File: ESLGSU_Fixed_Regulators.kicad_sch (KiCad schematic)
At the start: 0 parts

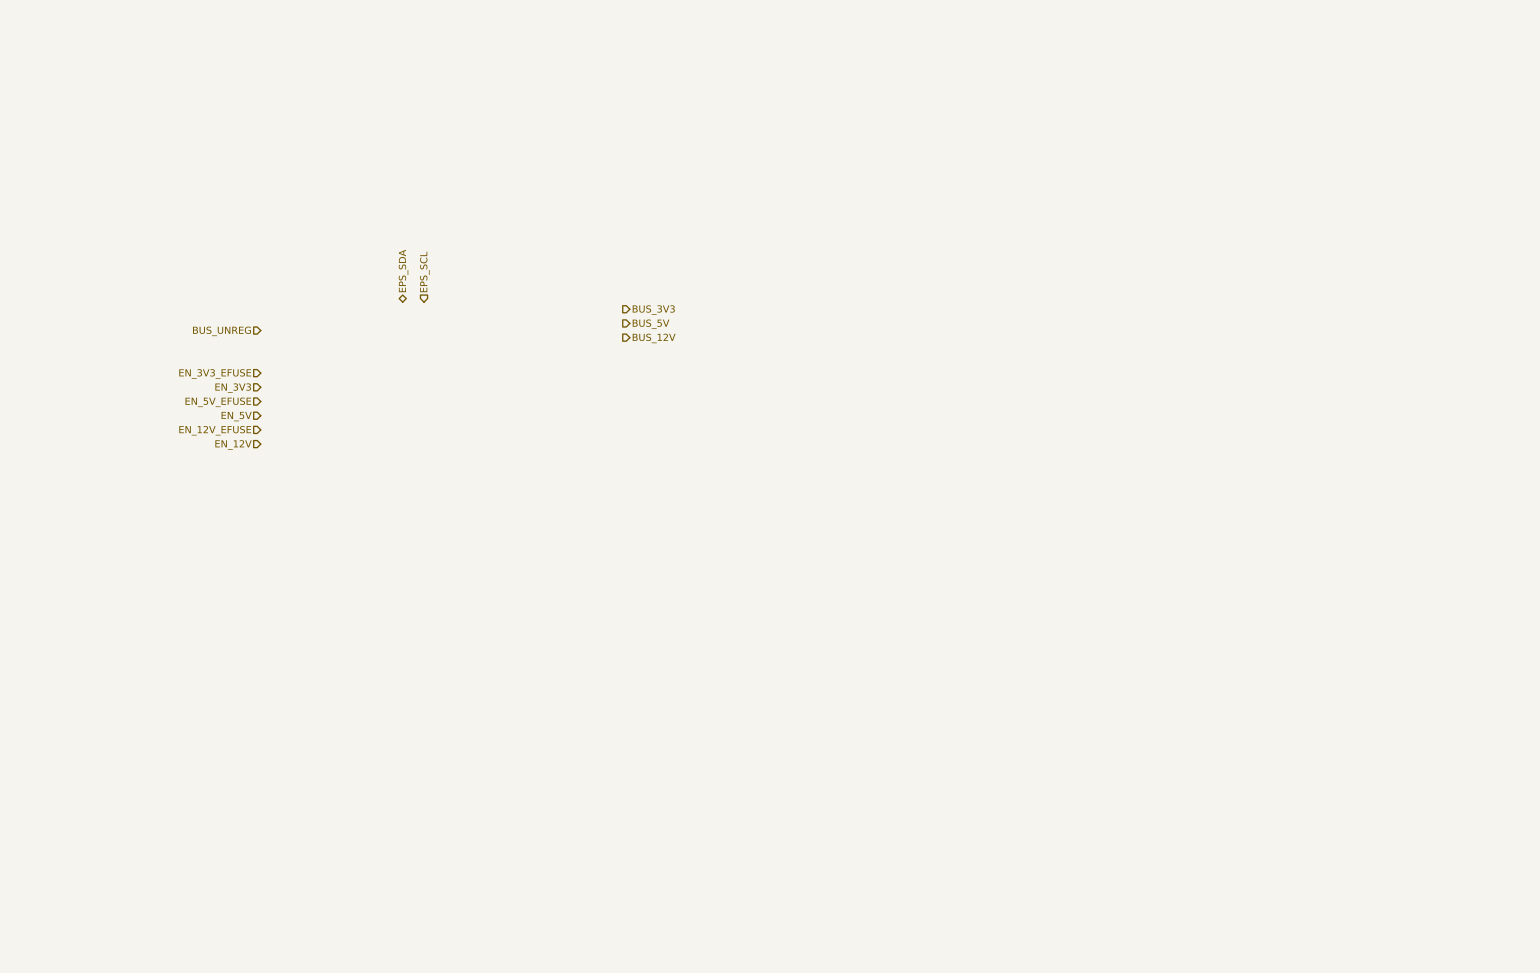
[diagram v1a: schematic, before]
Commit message: Additional power regulation work
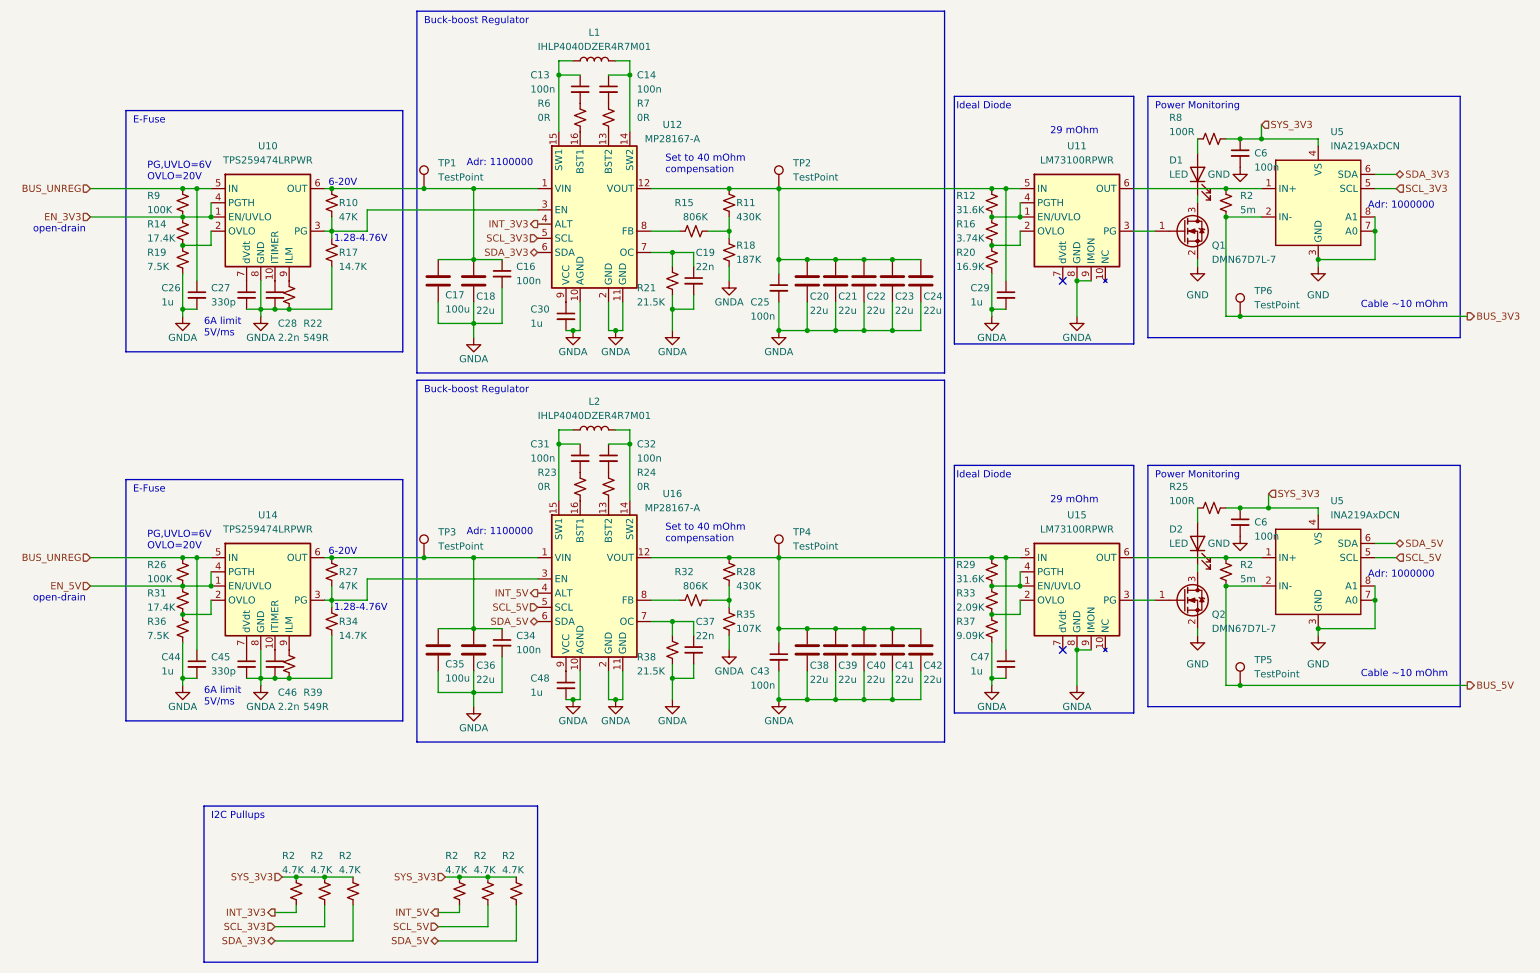
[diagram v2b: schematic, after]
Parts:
- added C13, C14, C16, C25, C31, C32, C34, C43, C6 (x2): 100n, Capacitor_SMD:C_0603_1608Metric, symbol Device:C_Small
- added C17, C35: 100u, Capacitor_SMD:CP_Elec_6.3x7.7, symbol Device:C
- added C18, C20, C21, C22, C23, C24, C36, C38, C39, C40, C41, C42: 22u, Capacitor_SMD:C_0805_2012Metric, symbol Device:C
- added C19, C37: 22n, Capacitor_SMD:C_0603_1608Metric, symbol Device:C_Small
- added C26, C29, C30, C44, C47, C48: 1u, Capacitor_SMD:C_0603_1608Metric, symbol Device:C_Small
- added C27, C45: 330p, Capacitor_SMD:C_0603_1608Metric, symbol Device:C_Small
- added C28, C46: 2.2n, Capacitor_SMD:C_0603_1608Metric, symbol Device:C_Small
- added D1, D2: LED, LED_SMD:LED_0603_1608Metric, symbol Device:LED
- added L1, L2: IHLP4040DZER4R7M01, Inductor_SMD:L_Vishay_IHLP-4040, symbol Device:L
- added Q1, Q2: DMN67D7L-7, Package_TO_SOT_SMD:SOT-323_SC-70, symbol Transistor_FET:DMN67D7L
- added R10, R27: 47K, Resistor_SMD:R_0603_1608Metric, symbol Device:R_Small_US
- added R11, R28: 430K, Resistor_SMD:R_0603_1608Metric, symbol Device:R_Small_US
- added R12, R29: 31.6K, Resistor_SMD:R_0603_1608Metric, symbol Device:R_Small_US
- added R14, R31: 17.4K, Resistor_SMD:R_0603_1608Metric, symbol Device:R_Small_US
- added R15, R32: 806K, Resistor_SMD:R_0603_1608Metric, symbol Device:R_Small_US
- added R16: 3.74K, Resistor_SMD:R_0603_1608Metric, symbol Device:R_Small_US
- added R17, R34: 14.7K, Resistor_SMD:R_0603_1608Metric, symbol Device:R_Small_US
- added R18: 187K, Resistor_SMD:R_0603_1608Metric, symbol Device:R_Small_US
- added R19, R36: 7.5K, Resistor_SMD:R_0603_1608Metric, symbol Device:R_Small_US
- added R2 (x6): 4.7K, Resistor_SMD:R_0603_1608Metric, symbol Device:R_Small_US
- added R2 (x2): 5m, Resistor_SMD:R_0603_1608Metric, symbol Device:R_Small_US
- added R20: 16.9K, Resistor_SMD:R_0603_1608Metric, symbol Device:R_Small_US
- added R21, R38: 21.5K, Resistor_SMD:R_0603_1608Metric, symbol Device:R_Small_US
- added R22, R39: 549R, Resistor_SMD:R_0603_1608Metric, symbol Device:R_Small_US
- added R23, R24, R6, R7: 0R, Resistor_SMD:R_0603_1608Metric, symbol Device:R_Small_US
- added R25, R8: 100R, Resistor_SMD:R_0603_1608Metric, symbol Device:R_Small_US
- added R26, R9: 100K, Resistor_SMD:R_0603_1608Metric, symbol Device:R_Small_US
- added R33: 2.09K, Resistor_SMD:R_0603_1608Metric, symbol Device:R_Small_US
- added R35: 107K, Resistor_SMD:R_0603_1608Metric, symbol Device:R_Small_US
- added R37: 9.09K, Resistor_SMD:R_0603_1608Metric, symbol Device:R_Small_US
- added TP1, TP2, TP3, TP4, TP5, TP6: TestPoint, TestPoint:TestPoint_Pad_D2.0mm, symbol Connector:TestPoint
- added U10, U14: TPS259474LRPWR, ESLGSU_Parts_Lib:VQFN-HR, symbol ESLGSU_Parts_Lib:TPS259474ARPWR
- added U11, U15: LM73100RPWR, ESLGSU_Parts_Lib:VQFN-HR, symbol ESLGSU_Parts_Lib:LM73100
- added U12, U16: MP28167-A, ESLGSU_Parts_Lib:QFN-16-MP28167, symbol ESLGSU_Parts_Lib:MP28167-A
- added U5 (x2): INA219AxDCN, Package_TO_SOT_SMD:SOT-23-8, symbol Sensor_Energy:INA219AxDCN
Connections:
- net BUS_3V3: now also R2.2, TP6.1, U5.2 (IN-)
- net BUS_5V: now also R2.2, TP5.1, U5.2 (IN-)
- net BUS_UNREG: now also C26.1, C44.1, R26.1, R9.1, U10.5 (IN), U14.5 (IN)
- net EN_3V3: now also R14.1, R9.2, U10.1 (EN/UVLO), U10.4 (PGTH)
- net EN_5V: now also R26.2, R31.1, U14.1 (EN/UVLO), U14.4 (PGTH)
- new net: C14.1, L1.2, U12.14 (SW2)
- new net: C14.2, R7.1
- new net: C20.1, C21.1, C22.1, C23.1, C24.1, C25.1, C29.1, R11.1, R12.1, TP2.1, U11.5 (IN), U12.12 (VOUT)
- new net: R11.2, R15.2, R18.1
- new net: C27.1, U10.7 (dVdt)
- new net: C13.1, L1.1, U12.15 (SW1)
- new net: C38.1, C39.1, C40.1, C41.1, C42.1, C43.1, C47.1, R28.1, R29.1, TP4.1, U15.5 (IN), U16.12 (VOUT)
- new net: C34.1, C35.1, C36.1, R27.1, TP3.1, U14.6 (OUT), U16.1 (VIN)
- new net: R31.2, R36.1, U14.2 (OVLO)
- new net: C13.2, R6.1
- new net: C16.1, C17.1, C18.1, R10.1, TP1.1, U10.6 (OUT), U12.1 (VIN)
- new net: R14.2, R19.1, U10.2 (OVLO)
- new net: R10.2, R17.1, U10.3 (PG), U12.3 (EN)
- new net: C31.1, L2.1, U16.15 (SW1)
- new net: C32.1, L2.2, U16.14 (SW2)
- new net: D2.2 (A), R25.2
- new net: C28.1, U10.10 (ITIMER)
- new net: C48.1, U16.9 (VCC)
- new net: R2.1, U11.6 (OUT), U5.1 (IN+)
- new net: R7.2, U12.13 (BST2)
- new net: R2.1, U15.6 (OUT), U5.1 (IN+)
- new net: R12.2, R16.1, U11.1 (EN/UVLO), U11.4 (PGTH)
- new net: R16.2, R20.1, U11.2 (OVLO)
- new net: R22.1, U10.9 (ILM)
- new net: R39.1, U14.9 (ILM)
- new net: R28.2, R32.2, R35.1
- new net: D1.2 (A), R8.2
- new net: R27.2, R34.1, U14.3 (PG), U16.3 (EN)
- new net: C30.1, U12.9 (VCC)
- new net: C19.1, R21.1, U12.7 (OC)
- new net: D2.1 (K), Q2.3 (D)
- new net: Q1.1 (G), U11.3 (PG)
- new net: C46.1, U14.10 (ITIMER)
- new net: C32.2, R24.1
- new net: R24.2, U16.13 (BST2)
- new net: R23.2, U16.16 (BST1)
- new net: C37.1, R38.1, U16.7 (OC)
- new net: R32.1, U16.8 (FB)
- new net: R6.2, U12.16 (BST1)
- new net: R15.1, U12.8 (FB)
- new net: C31.2, R23.1
- new net: D1.1 (K), Q1.3 (D)
- new net: R29.2, R33.1, U15.1 (EN/UVLO), U15.4 (PGTH)
- new net: R33.2, R37.1, U15.2 (OVLO)
- new net: Q2.1 (G), U15.3 (PG)
- new net: C45.1, U14.7 (dVdt)
- new net GND: C6.2, C6.2, Q1.2 (S), Q2.2 (S), U5.3 (GND), U5.3 (GND), U5.7 (A0), U5.7 (A0), U5.8 (A1), U5.8 (A1)
- new net GNDA: C16.2, C17.2, C18.2, C19.2, C20.2, C21.2, C22.2, C23.2, C24.2, C25.2, C26.2, C27.2, C28.2, C29.2, C30.2, C34.2, C35.2, C36.2, C37.2, C38.2, C39.2, C40.2, C41.2, C42.2, C43.2, C44.2, C45.2, C46.2, C47.2, C48.2, R17.2, R18.2, R19.2, R20.2, R21.2, R22.2, R34.2, R35.2, R36.2, R37.2, R38.2, R39.2, U10.8 (GND), U11.8 (GND), U11.9 (IMON), U12.10 (AGND), U12.11 (GND), U12.2 (GND), U14.8 (GND), U15.8 (GND), U15.9 (IMON), U16.10 (AGND), U16.11 (GND), U16.2 (GND)
- new net INT_3V3: R2.2, U12.4 (ALT)
- new net INT_5V: R2.2, U16.4 (ALT)
- new net SCL_3V3: R2.2, U12.5 (SCL), U5.5 (SCL)
- new net SCL_5V: R2.2, U16.5 (SCL), U5.5 (SCL)
- new net SDA_3V3: R2.2, U12.6 (SDA), U5.6 (SDA)
- new net SDA_5V: R2.2, U16.6 (SDA), U5.6 (SDA)
- new net SYS_3V3: C6.1, C6.1, R2.1, R2.1, R2.1, R2.1, R2.1, R2.1, R25.1, R8.1, U5.4 (VS), U5.4 (VS)
- no-connect marks 0 -> 2
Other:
- note added: "1.28-4.76V"
- note added: "29 mOhm"
- note added: "6-20V"
- note added: "6A limit 5V/ms"
- note added: "Adr: 1000000"
- note added: "Adr: 1100000"
- note added: "Buck-boost Regulator"
- note added: "Cable ~10 mOhm"
- note added: "E-Fuse"
- note added: "I2C Pullups"
- note added: "Ideal Diode"
- note added: "PG,UVLO=6V OVLO=20V"
- note added: "Power Monitoring"
- note added: "Set to 40 mOhm compensation"
- note added: "open-drain"

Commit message: Added 5v/3V3 regulators and mux
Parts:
- added R87, R88: 47K, Resistor_SMD:R_0603_1608Metric, symbol Device:R_Small_US
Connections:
- net at D2.2 (A), R25.2: now also R88.1
- net at D1.2 (A), R8.2: now also R87.1
- net at Q1.1 (G), U11.3 (PG): now also R87.2
- net at Q2.1 (G), U15.3 (PG): now also R88.2
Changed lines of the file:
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@@
   (junction (at 204.47 62.23) (diameter 0) (color 0 0 0 0)
   )
+  (junction (at 226.06 102.87) (diameter 0) (color 0 0 0 0)
+  )
   (junction (at 151.13 111.76) (diameter 0) (color 0 0 0 0)
   )
@@
   (junction (at 132.08 67.31) (diameter 0) (color 0 0 0 0)
   )
+  (junction (at 218.44 119.38) (diameter 0) (color 0 0 0 0)
+  )
   (junction (at 44.45 45.72) (diameter 0) (color 0 0 0 0)
   )
+  (junction (at 226.06 36.83) (diameter 0) (color 0 0 0 0)
+  )
   (junction (at 142.24 119.38) (diameter 0) (color 0 0 0 0)
   )
@@
   (junction (at 233.68 68.58) (diameter 0) (color 0 0 0 0)
   )
+  (junction (at 218.44 53.34) (diameter 0) (color 0 0 0 0)
+  )
   (junction (at 151.13 71.12) (diameter 0) (color 0 0 0 0)
   )
@@
     (stroke (width 0) (type default))
   )
+  (wire (pts (xy 220.98 36.83) (xy 218.44 36.83))
+    (stroke (width 0) (type default))
+  )
   (wire (pts (xy 231.14 50.8) (xy 237.49 50.8))
     (stroke (width 0) (type default))
@@
     (stroke (width 0) (type default))
   )
+  (wire (pts (xy 220.98 102.87) (xy 218.44 102.87))
+    (stroke (width 0) (type default))
+  )
   (wire (pts (xy 44.45 67.31) (xy 44.45 68.58))
     (stroke (width 0) (type default))
@@
     (stroke (width 0) (type default))
   )
+  (wire (pts (xy 218.44 102.87) (xy 218.44 119.38))
+    (stroke (width 0) (type default))
+  )
   (wire (pts (xy 231.14 36.83) (xy 233.68 36.83))
     (stroke (width 0) (type default))
@@
     (stroke (width 0) (type default))
   )
+  (wire (pts (xy 218.44 36.83) (xy 218.44 53.34))
+    (stroke (width 0) (type default))
+  )
   (wire (pts (xy 171.45 124.46) (xy 176.53 124.46))
     (stroke (width 0) (type default))
@@
     (effects (font (size 1.27 1.27)) (justify left))
   )
+  (symbol (lib_id "Device:R_Small_US") (at 223.52 36.83 270) (unit 1)
+    (in_bom yes) (on_board yes) (dnp no)
+    (property "Reference" "R87" (at 217.4449 32.9491 90)
+      (effects (font (size 1.27 1.27)) (justify left))
+    )
+    (property "Value" "47K" (at 217.4449 35.4891 90)
+      (effects (font (size 1.27 1.27)) (justify left))
+    )
+    (property "Footprint" "Resistor_SMD:R_0603_1608Metric" (at 223.52 36.83 0)
+      (effects (font (size 1.27 1.27)) hide)
+    )
+    (property "Datasheet" "~" (at 223.52 36.83 0)
+      (effects (font (size 1.27 1.27)) hide)
+    )
+    (pin "1")
+    (pin "2")
+    (instances
+      (project "ESLGSU"
+        (path "/b556fa32-e0cb-409c-ac85-9f2ac606be79/09a64186-e4de-4db7-b903-c6397ff9a54d"
+          (reference "R87") (unit 1)
+        )
+      )
+    )
+  )
   (symbol (lib_id "power:GNDA") (at 189.23 68.58 0) (unit 1)
     (in_bom yes) (on_board yes) (dnp no)
@@
     )
   )
+  (symbol (lib_id "Device:R_Small_US") (at 223.52 102.87 270) (unit 1)
+    (in_bom yes) (on_board yes) (dnp no)
+    (property "Reference" "R88" (at 217.4449 98.9891 90)
+      (effects (font (size 1.27 1.27)) (justify left))
+    )
+    (property "Value" "47K" (at 217.4449 101.5291 90)
+      (effects (font (size 1.27 1.27)) (justify left))
+    )
+    (property "Footprint" "Resistor_SMD:R_0603_1608Metric" (at 223.52 102.87 0)
+      (effects (font (size 1.27 1.27)) hide)
+    )
+    (property "Datasheet" "~" (at 223.52 102.87 0)
+      (effects (font (size 1.27 1.27)) hide)
+    )
+    (pin "1")
+    (pin "2")
+    (instances
+      (project "ESLGSU"
+        (path "/b556fa32-e0cb-409c-ac85-9f2ac606be79/09a64186-e4de-4db7-b903-c6397ff9a54d"
+          (reference "R88") (unit 1)
+        )
+      )
+    )
+  )
   (symbol (lib_id "Device:C") (at 161.29 62.23 0) (unit 1)
     (in_bom yes) (on_board yes) (dnp no)
@@
   (symbol (lib_id "Device:R_Small_US") (at 228.6 102.87 270) (unit 1)
     (in_bom yes) (on_board yes) (dnp no)
-    (property "Reference" "R25" (at 220.98 99.06 90)
+    (property "Reference" "R25" (at 229.87 99.06 90)
       (effects (font (size 1.27 1.27)) (justify left))
     )
-    (property "Value" "100R" (at 220.98 101.6 90)
+    (property "Value" "100R" (at 229.87 101.6 90)
       (effects (font (size 1.27 1.27)) (justify left))
     )
@@
     )
   )
-  (symbol (lib_id "Device:R_Small_US") (at 228.6 36.83 270) (unit 1)
-    (in_bom yes) (on_board yes) (dnp no)
-    (property "Reference" "R8" (at 220.98 33.02 90)
-      (effects (font (size 1.27 1.27)) (justify left))
-    )
-    (property "Value" "100R" (at 220.98 35.56 90)
-      (effects (font (size 1.27 1.27)) (justify left))
-    )
-    (property "Footprint" "Resistor_SMD:R_0603_1608Metric" (at 228.6 36.83 0)
-      (effects (font (size 1.27 1.27)) hide)
-    )
-    (property "Datasheet" "~" (at 228.6 36.83 0)
-      (effects (font (size 1.27 1.27)) hide)
-    )
-    (pin "1")
-    (pin "2")
-    (instances
-      (project "ESLGSU"
-        (path "/b556fa32-e0cb-409c-ac85-9f2ac606be79/09a64186-e4de-4db7-b903-c6397ff9a54d"
-          (reference "R8") (unit 1)
-        )
-      )
-    )
-  )
   (symbol (lib_id "power:GNDA") (at 142.24 128.27 0) (unit 1)
     (in_bom yes) (on_board yes) (dnp no)
@@
         )
       )
+    )
+  )
+  (symbol (lib_id "Device:R_Small_US") (at 228.6 36.83 270) (unit 1)
+    (in_bom yes) (on_board yes) (dnp no)
+    (property "Reference" "R8" (at 229.8537 33.1656 90)
+      (effects (font (size 1.27 1.27)) (justify left))
+    )
+    (property "Value" "100R" (at 229.8537 35.7056 90)
+      (effects (font (size 1.27 1.27)) (justify left))
+    )
+    (property "Footprint" "Resistor_SMD:R_0603_1608Metric" (at 228.6 36.83 0)
+      (effects (font (size 1.27 1.27)) hide)
+    )
+    (property "Datasheet" "~" (at 228.6 36.83 0)
+      (effects (font (size 1.27 1.27)) hide)
+    )
+    (pin "1")
+    (pin "2")
+    (instances
+      (project "ESLGSU"
+        (path "/b556fa32-e0cb-409c-ac85-9f2ac606be79/09a64186-e4de-4db7-b903-c6397ff9a54d"
+          (reference "R8") (unit 1)
+        )
+      )

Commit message: uC Interface work
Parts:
- Q1, Q2: footprint Package_TO_SOT_SMD:SOT-323_SC-70 -> Package_TO_SOT_SMD:SOT-23
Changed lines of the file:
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@@
     )
   )
-  (symbol (lib_id "ESLGSU_Parts_Lib:LM73100") (at 204.47 50.8 0) (unit 1)
+  (symbol (lib_id "ESLGSU_Parts_Lib:LM73100") (at 204.47 49.53 0) (unit 1)
     (in_bom yes) (on_board yes) (dnp no) (fields_autoplaced)
-    (property "Reference" "U11" (at 204.47 38.1 0)
-      (effects (font (size 1.27 1.27)))
-    )
-    (property "Value" "LM73100RPWR" (at 204.47 40.64 0)
-      (effects (font (size 1.27 1.27)))
-    )
-    (property "Footprint" "ESLGSU_Parts_Lib:VQFN-HR" (at 203.2 69.85 0)
-      (effects (font (size 1.27 1.27)) hide)
-    )
-    (property "Datasheet" "" (at 204.47 50.8 0)
+    (property "Reference" "U11" (at 204.47 36.83 0)
+      (effects (font (size 1.27 1.27)))
+    )
+    (property "Value" "LM73100RPWR" (at 204.47 39.37 0)
+      (effects (font (size 1.27 1.27)))
+    )
+    (property "Footprint" "ESLGSU_Parts_Lib:VQFN-HR" (at 203.2 68.58 0)
+      (effects (font (size 1.27 1.27)) hide)
+    )
+    (property "Datasheet" "" (at 204.47 49.53 0)
       (effects (font (size 1.27 1.27)) hide)
     )
@@
       (effects (font (size 1.27 1.27)) (justify left))
     )
-    (property "Footprint" "Package_TO_SOT_SMD:SOT-323_SC-70" (at 228.6 55.245 0)
+    (property "Footprint" "Package_TO_SOT_SMD:SOT-23" (at 228.6 55.245 0)
       (effects (font (size 1.27 1.27) italic) (justify left) hide)
     )
@@
       (effects (font (size 1.27 1.27)) (justify left))
     )
-    (property "Footprint" "Package_TO_SOT_SMD:SOT-323_SC-70" (at 228.6 121.285 0)
+    (property "Footprint" "Package_TO_SOT_SMD:SOT-23" (at 228.6 121.285 0)
       (effects (font (size 1.27 1.27) italic) (justify left) hide)
     )
@@
     )
   )
-  (symbol (lib_id "ESLGSU_Parts_Lib:LM73100") (at 204.47 116.84 0) (unit 1)
+  (symbol (lib_id "ESLGSU_Parts_Lib:LM73100") (at 204.47 115.57 0) (unit 1)
     (in_bom yes) (on_board yes) (dnp no) (fields_autoplaced)
-    (property "Reference" "U15" (at 204.47 104.14 0)
-      (effects (font (size 1.27 1.27)))
-    )
-    (property "Value" "LM73100RPWR" (at 204.47 106.68 0)
-      (effects (font (size 1.27 1.27)))
-    )
-    (property "Footprint" "ESLGSU_Parts_Lib:VQFN-HR" (at 203.2 135.89 0)
-      (effects (font (size 1.27 1.27)) hide)
-    )
-    (property "Datasheet" "" (at 204.47 116.84 0)
-      (effects (font (size 1.27 1.27)) hide)
-    )
+    (property "Reference" "U15" (at 204.47 102.87 0)
+      (effects (font (size 1.27 1.27)))
+    )
+    (property "Value" "LM73100RPWR" (at 204.47 105.41 0)
+      (effects (font (size 1.27 1.27)))
+    )
+    (property "Footprint" "ESLGSU_Parts_Lib:VQFN-HR" (at 203.2 134.62 0)
+      (effects (font (size 1.27 1.27)) hide)
+    )
+    (property "Datasheet" "" (at 204.47 115.57 0)
+      (effects (font (size 1.27 1.27)) hide)
+    )

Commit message: Finished interfaces work
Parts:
- C13, C14, C16, C19, C25, C26, C27, C28, C29, C30, C31, C32, C34, C37, C43, C44, C45, C46, C47, C48, C6: footprint Capacitor_SMD:C_0603_1608Metric -> Capacitor_SMD:C_0402_1005Metric
- R10, R11, R12, R14, R15, R16, R17, R18, R19, R2, R20, R21, R22, R23, R24, R25, R26, R27, R28, R29, R31, R32, R33, R34, R35, R36, R37, R38, R39, R6, R7, R8, R87, R88, R9: footprint Resistor_SMD:R_0603_1608Metric -> Resistor_SMD:R_0402_1005Metric
